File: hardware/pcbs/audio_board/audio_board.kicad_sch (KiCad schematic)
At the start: 16 parts, among them J11 Conn_01x08, J4 NC3MAH, J5 NC3MAH, J6 AudioJack3, J8 I2C

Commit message: fix libraries
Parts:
- removed U4: ~, Library:Teensy41, symbol Parts:Teensy41
- added R7, R8: 47, Resistor_SMD:R_0805_2012Metric, symbol Device:R
- added U1: ~, extra:Teensy41, symbol extra:Teensy41
- J2: renamed from J11; footprint Library:mta100_01x8_P2.54_647050-8 -> Connector_MTA-100:mta100_01x8_P2.54_647050-8
- renumbered H3 to H2, H2 to H3, J8 to J1, J4 to J3, J6 to J4, R11 to R1, R12 to R2, R13 to R3, R14 to R4, R71 to R5, R72 to R6
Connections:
- net +3V3 is gone; now on net +3.3V: J1.1 (Pin_1), J2.8 (Pin_8), R1.1, R2.1, R3.1, R4.1
- net +3.3V: now also U1.3V (3v3)
- net +5V: now also U1.5V (Vin)
- net CS_LEFT: now also U1.9
- net CS_RIGHT: now also U1.10
- net DC: now also U1.12
- net DECT_INT: now also U1.33
- net DECT_RESET: now also U1.34
- net DECT_RX: now also U1.15
- net DECT_TX: now also U1.14
- net GND: now also U1.G (GND)
- net HP_GND: now also R8.1; no longer J4.S
- net I2S1_BCLK: now also U1.21
- net I2S1_LRCLK: now also U1.20
- net I2S1_MCLK: now also U1.23
- net I2S1_RX1: now also U1.8
- net I2S1_RX2: now also U1.6
- net I2S1_TX1: now also U1.7
- net I2S1_TX2: now also U1.32
- net I2S2_BCLK: now also U1.4
- net I2S2_FS: now also U1.3
- net I2S2_RX: now also U1.5
- net I2S2_TX: now also U1.2
- net MOSI: now also U1.11
- net PHANTOM_IN1_EN: now also U1.37
- net PHANTOM_IN2_EN: now also U1.36
- net PHANTOM_IN3_EN: now also U1.35
- net RESET: now also U1.24
- net SCK: now also U1.13
- net SCL: now also U1.19
- net SCL1: now also U1.16
- net SDA: now also U1.18
- net SDA1: now also U1.17
- new net: J4.S, R7.2, R8.2
- new net DAC 2/OUTA-: R7.1
- no-connect marks 2 -> 23
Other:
- moved on the sheet: J1, J2, J3, J4, J5, R1, R2, R3, R4, R5, R6

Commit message: final touches to libraries
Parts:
- J3, J5: footprint Library:Jack_XLR_Neutrik_NC3MAH_Horizontal -> conn:Jack_XLR_Neutrik_NC3MAH_Horizontal
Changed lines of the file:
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@@
 			)
 		)
-		(property "Footprint" "Library:Jack_XLR_Neutrik_NC3MAH_Horizontal"
+		(property "Footprint" "conn:Jack_XLR_Neutrik_NC3MAH_Horizontal"
 			(at 212.09 85.09 0)
 			(effects
@@
 			)
 		)
-		(property "Footprint" "Library:Jack_XLR_Neutrik_NC3MAH_Horizontal"
+		(property "Footprint" "conn:Jack_XLR_Neutrik_NC3MAH_Horizontal"
 			(at 184.15 85.09 0)
 			(effects

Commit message: some more routing
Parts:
- added R9: 0, Resistor_SMD:R_0805_2012Metric, symbol Device:R
- R7, R8: value 47 -> 0
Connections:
- net GND: now also R9.1
- net at J4.S, R7.2, R8.2: now also R9.2
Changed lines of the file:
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@@
 	(text "OUTB- close to connector"
 		(exclude_from_sim no)
-		(at 185.166 143.51 0)
+		(at 191.77 128.27 0)
 		(effects
 			(font
@@
 	(wire
 		(pts
+			(xy 177.8 148.59) (xy 177.8 149.86)
+		)
+		(stroke
+			(width 0)
+			(type default)
+		)
+	)
+	(wire
+		(pts
 			(xy 25.4 80.01) (xy 35.56 80.01)
 		)
@@
 	(wire
 		(pts
+			(xy 177.8 138.43) (xy 177.8 140.97)
+		)
+		(stroke
+			(width 0)
+			(type default)
+		)
+	)
+	(wire
+		(pts
 			(xy 25.4 69.85) (xy 35.56 69.85)
 		)
@@
 	(symbol
 		(lib_id "power:GND")
+		(at 177.8 149.86 0)
+		(unit 1)
+		(exclude_from_sim no)
+		(in_bom yes)
+		(on_board yes)
+		(dnp no)
+		(fields_autoplaced yes)
+		(property "Reference" "#PWR013"
+			(at 177.8 156.21 0)
+			(effects
+				(font
+					(size 1.27 1.27)
+				)
+				(hide yes)
+			)
+		)
+		(property "Value" "GND"
+			(at 177.8 154.3034 0)
+			(effects
+				(font
+					(size 1.27 1.27)
+				)
+				(hide yes)
+			)
+		)
+		(property "Footprint" ""
+			(at 177.8 149.86 0)
+			(effects
+				(font
+					(size 1.27 1.27)
+				)
+				(hide yes)
+			)
+		)
+		(property "Datasheet" ""
+			(at 177.8 149.86 0)
+			(effects
+				(font
+					(size 1.27 1.27)
+				)
+				(hide yes)
+			)
+		)
+		(property "Description" ""
+			(at 177.8 149.86 0)
+			(effects
+				(font
+					(size 1.27 1.27)
+				)
+				(hide yes)
+			)
+		)
+		(pin "1"
+		)
+		(instances
+			(project "audio_board"
+				(path "/54443f96-c7c5-4432-b890-45b14a1547a1"
+					(reference "#PWR013")
+					(unit 1)
+				)
+			)
+		)
+	)
+	(symbol
+		(lib_id "power:GND")
 		(at 165.1 67.31 0)
 		(unit 1)
@@
 		(dnp no)
 		(fields_autoplaced yes)
-		(property "Reference" "#PWR016"
+		(property "Reference" "#PWR017"
 			(at 259.08 144.78 0)
 			(effects
@@
 			(project "audio_board"
 				(path "/54443f96-c7c5-4432-b890-45b14a1547a1"
-					(reference "#PWR016")
+					(reference "#PWR017")
 					(unit 1)
 				)
@@
 		(dnp no)
 		(fields_autoplaced yes)
-		(property "Reference" "#PWR017"
+		(property "Reference" "#PWR018"
 			(at 259.08 157.48 0)
 			(effects
@@
 			(project "audio_board"
 				(path "/54443f96-c7c5-4432-b890-45b14a1547a1"
-					(reference "#PWR017")
+					(reference "#PWR018")
 					(unit 1)
 				)
@@
 		(dnp no)
 		(fields_autoplaced yes)
-		(property "Reference" "#PWR015"
+		(property "Reference" "#PWR016"
 			(at 234.95 157.48 0)
 			(effects
@@
 			(project "audio_board"
 				(path "/54443f96-c7c5-4432-b890-45b14a1547a1"
-					(reference "#PWR015")
+					(reference "#PWR016")
 					(unit 1)
 				)
@@
 			)
 		)
-		(property "Value" "47"
+		(property "Value" "0"
 			(at 171.196 133.35 90)
 			(effects
@@
 		(dnp no)
 		(fields_autoplaced yes)
-		(property "Reference" "#PWR013"
+		(property "Reference" "#PWR014"
 			(at 203.2 101.6 0)
 			(effects
@@
 			(project "audio_board"
 				(path "/54443f96-c7c5-4432-b890-45b14a1547a1"
-					(reference "#PWR013")
+					(reference "#PWR014")
 					(unit 1)
 				)
@@
 		(dnp no)
 		(fields_autoplaced yes)
-		(property "Reference" "#PWR014"
+		(property "Reference" "#PWR015"
 			(at 234.95 144.78 0)
 			(effects
@@
 			(project "audio_board"
 				(path "/54443f96-c7c5-4432-b890-45b14a1547a1"
-					(reference "#PWR014")
+					(reference "#PWR015")
 					(unit 1)
 				)
@@
 	(symbol
 		(lib_id "Device:R")
+		(at 177.8 144.78 180)
+		(unit 1)
+		(exclude_from_sim no)
+		(in_bom yes)
+		(on_board yes)
+		(dnp yes)
+		(property "Reference" "R9"
+			(at 180.34 143.51 0)
+			(effects
+				(font
+					(size 1.27 1.27)
+				)
+			)
+		)
+		(property "Value" "0"
+			(at 180.34 146.05 0)
+			(effects
+				(font
+					(size 1.27 1.27)
+				)
+			)
+		)
+		(property "Footprint" "Resistor_SMD:R_0805_2012Metric"
+			(at 179.578 144.78 90)
+			(effects
+				(font
+					(size 1.27 1.27)
+				)
+				(hide yes)
+			)
+		)
+		(property "Datasheet" "~"
+			(at 177.8 144.78 0)
+			(effects
+				(font
+					(size 1.27 1.27)
+				)
+				(hide yes)
+			)
+		)
+		(property "Description" "Resistor"
+			(at 177.8 144.78 0)
+			(effects
+				(font
+					(size 1.27 1.27)
+				)
+				(hide yes)
+			)
+		)
+		(property "LCSC" "C23182"
+			(at 177.8 144.78 0)
+			(effects
+				(font
+					(size 1.27 1.27)
+				)
+				(hide yes)
+			)
+		)
+		(property "MPN" "560112116054"
+			(at 177.8 144.78 0)
+			(effects
+				(font
+					(size 1.27 1.27)
+				)
+				(hide yes)
+			)
+		)
+		(property "Part" "R 47Ω 125mW 1% 0603"
+			(at 177.8 144.78 0)
+			(effects
+				(font
+					(size 1.27 1.27)
+				)
+				(hide yes)
+			)
+		)
+		(property "Shop" "https://store.comet.bg/Catalogue/Product/4392/"
+			(at 177.8 144.78 0)
+			(effects
+				(font
+					(size 1.27 1.27)
+				)
+				(hide yes)
+			)
+		)
+		(pin "1"
+		)
+		(pin "2"
+		)
+		(instances
+			(project "audio_board"
+				(path "/54443f96-c7c5-4432-b890-45b14a1547a1"
+					(reference "R9")
+					(unit 1)
+				)
+			)
+		)
+	)
+	(symbol
+		(lib_id "Device:R")
 		(at 171.45 138.43 90)
 		(unit 1)
@@
 			)
 		)
-		(property "Value" "47"
+		(property "Value" "0"
 			(at 171.196 138.43 90)
 			(effects

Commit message: route some more
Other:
- sheet PC Mono input ports: added OUT+, OUT-; removed OUTPUT
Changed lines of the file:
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@@
 	(wire
 		(pts
+			(xy 165.1 63.5) (xy 187.96 63.5)
+		)
+		(stroke
+			(width 0)
+			(type default)
+		)
+	)
+	(wire
+		(pts
 			(xy 44.45 22.86) (xy 44.45 24.13)
 		)
@@
 	(wire
 		(pts
-			(xy 165.1 46.99) (xy 165.1 67.31)
+			(xy 165.1 46.99) (xy 165.1 63.5)
 		)
 		(stroke
@@
 		(dnp no)
 		(fields_autoplaced yes)
-		(property "Reference" "#PWR013"
+		(property "Reference" "#PWR012"
 			(at 177.8 156.21 0)
 			(effects
@@
 			(project "audio_board"
 				(path "/54443f96-c7c5-4432-b890-45b14a1547a1"
-					(reference "#PWR013")
-					(unit 1)
-				)
-			)
-		)
-	)
-	(symbol
-		(lib_id "power:GND")
-		(at 165.1 67.31 0)
-		(unit 1)
-		(exclude_from_sim no)
-		(in_bom yes)
-		(on_board yes)
-		(dnp no)
-		(fields_autoplaced yes)
-		(property "Reference" "#PWR011"
-			(at 165.1 73.66 0)
-			(effects
-				(font
-					(size 1.27 1.27)
-				)
-				(hide yes)
-			)
-		)
-		(property "Value" "GND"
-			(at 165.1 72.39 0)
-			(effects
-				(font
-					(size 1.27 1.27)
-				)
-				(hide yes)
-			)
-		)
-		(property "Footprint" ""
-			(at 165.1 67.31 0)
-			(effects
-				(font
-					(size 1.27 1.27)
-				)
-				(hide yes)
-			)
-		)
-		(property "Datasheet" ""
-			(at 165.1 67.31 0)
-			(effects
-				(font
-					(size 1.27 1.27)
-				)
-				(hide yes)
-			)
-		)
-		(property "Description" "Power symbol creates a global label with name \"GND\" , ground"
-			(at 165.1 67.31 0)
-			(effects
-				(font
-					(size 1.27 1.27)
-				)
-				(hide yes)
-			)
-		)
-		(pin "1"
-		)
-		(instances
-			(project ""
-				(path "/54443f96-c7c5-4432-b890-45b14a1547a1"
-					(reference "#PWR011")
+					(reference "#PWR012")
 					(unit 1)
 				)
@@
 		(dnp no)
 		(fields_autoplaced yes)
-		(property "Reference" "#PWR017"
+		(property "Reference" "#PWR016"
 			(at 259.08 144.78 0)
 			(effects
@@
 			(project "audio_board"
 				(path "/54443f96-c7c5-4432-b890-45b14a1547a1"
-					(reference "#PWR017")
+					(reference "#PWR016")
 					(unit 1)
 				)
@@
 		(dnp no)
 		(fields_autoplaced yes)
-		(property "Reference" "#PWR018"
+		(property "Reference" "#PWR017"
 			(at 259.08 157.48 0)
 			(effects
@@
 			(project "audio_board"
 				(path "/54443f96-c7c5-4432-b890-45b14a1547a1"
-					(reference "#PWR018")
+					(reference "#PWR017")
 					(unit 1)
 				)
@@
 		(dnp no)
 		(fields_autoplaced yes)
-		(property "Reference" "#PWR012"
+		(property "Reference" "#PWR011"
 			(at 175.26 101.6 0)
 			(effects
@@
 			(project "audio_board"
 				(path "/54443f96-c7c5-4432-b890-45b14a1547a1"
-					(reference "#PWR012")
+					(reference "#PWR011")
 					(unit 1)
 				)
@@
 		(dnp no)
 		(fields_autoplaced yes)
-		(property "Reference" "#PWR016"
+		(property "Reference" "#PWR015"
 			(at 234.95 157.48 0)
 			(effects
@@
 			(project "audio_board"
 				(path "/54443f96-c7c5-4432-b890-45b14a1547a1"
-					(reference "#PWR016")
+					(reference "#PWR015")
 					(unit 1)
 				)
@@
 		(dnp no)
 		(fields_autoplaced yes)
-		(property "Reference" "#PWR014"
+		(property "Reference" "#PWR013"
 			(at 203.2 101.6 0)
 			(effects
@@
 			(project "audio_board"
 				(path "/54443f96-c7c5-4432-b890-45b14a1547a1"
-					(reference "#PWR014")
+					(reference "#PWR013")
 					(unit 1)
 				)
@@
 		(dnp no)
 		(fields_autoplaced yes)
-		(property "Reference" "#PWR015"
+		(property "Reference" "#PWR014"
 			(at 234.95 144.78 0)
 			(effects
@@
 			(project "audio_board"
 				(path "/54443f96-c7c5-4432-b890-45b14a1547a1"
-					(reference "#PWR015")
+					(reference "#PWR014")
 					(unit 1)
 				)
@@
 	)
 	(sheet
-		(at 187.96 34.925)
+		(at 187.96 23.495)
 		(size 31.75 6.35)
 		(exclude_from_sim no)
@@
 		)
 		(property "Sheetname" "XLR input 2"
-			(at 187.96 34.2134 0)
+			(at 187.96 22.7834 0)
 			(effects
 				(font
@@
 		)
 		(property "Sheetfile" "xlr_input.kicad_sch"
-			(at 187.96 41.8596 0)
+			(at 187.96 30.4296 0)
 			(effects
 				(font
@@
 		)
 		(pin "COLD" output
-			(at 187.96 39.37 180)
+			(at 187.96 27.94 180)
 			(effects
 				(font
@@
 		)
 		(pin "HOT" output
-			(at 187.96 36.83 180)
+			(at 187.96 25.4 180)
 			(effects
 				(font
@@
 		)
 		(pin "PHANTOM_PULLDOWN" input
-			(at 219.71 36.83 0)
+			(at 219.71 25.4 0)
 			(effects
 				(font
@@
 	)
 	(sheet
-		(at 187.96 23.495)
+		(at 187.96 34.925)
 		(size 31.75 6.35)
 		(exclude_from_sim no)
@@
 		)
 		(property "Sheetname" "XLR input 1"
-			(at 187.96 22.7834 0)
+			(at 187.96 34.2134 0)
 			(effects
 				(font
@@
 		)
 		(property "Sheetfile" "xlr_input.kicad_sch"
-			(at 187.96 30.4296 0)
+			(at 187.96 41.8596 0)
 			(effects
 				(font
@@
 		)
 		(pin "COLD" output
-			(at 187.96 27.94 180)
+			(at 187.96 39.37 180)
 			(effects
 				(font
@@
 		)
 		(pin "HOT" output
-			(at 187.96 25.4 180)
+			(at 187.96 36.83 180)
 			(effects
 				(font
@@
 		)
 		(pin "PHANTOM_PULLDOWN" input
-			(at 219.71 25.4 0)
+			(at 219.71 36.83 0)
 			(effects
 				(font
@@
 	(sheet
 		(at 187.96 58.42)
-		(size 24.13 5.08)
+		(size 24.13 7.62)
 		(exclude_from_sim no)
 		(in_bom yes)
@@
 		)
 		(property "Sheetfile" "input_mono.kicad_sch"
-			(at 187.96 64.0846 0)
+			(at 187.96 66.6246 0)
 			(effects
 				(font
@@
 			)
 		)
-		(pin "OUTPUT" output
+		(pin "OUT+" output
 			(at 187.96 60.96 180)
 			(effects
 				(font
+					(size 1.27 1.27)
+				)
+				(justify left)
+			)
+		)
+		(pin "OUT-" output
+			(at 187.96 63.5 180)
+			(effects
+				(font

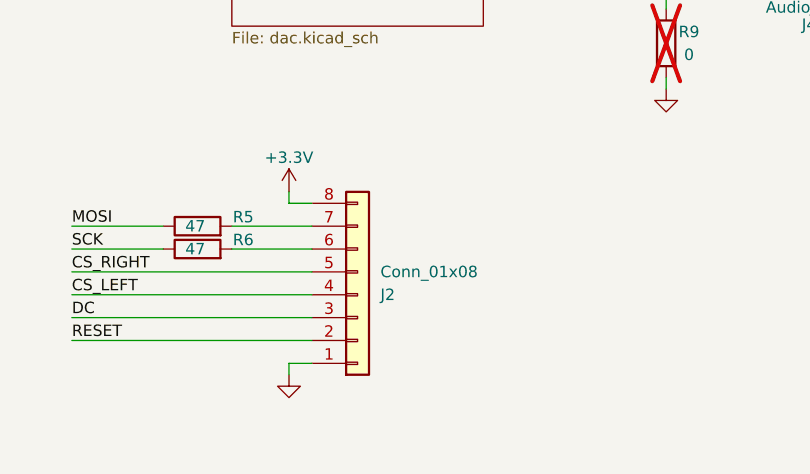
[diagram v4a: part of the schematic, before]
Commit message: fix XLR courtyard
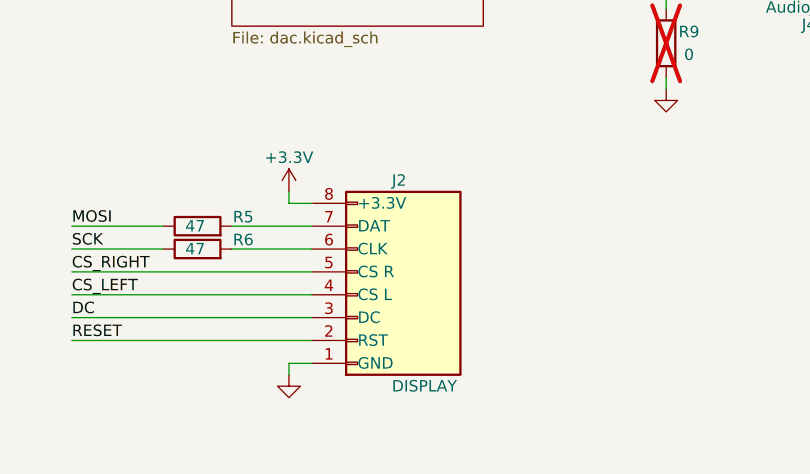
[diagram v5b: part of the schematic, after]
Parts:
- removed J2: Conn_01x08, Connector_MTA-100:mta100_01x8_P2.54_647050-8, symbol Connector_Generic:Conn_01x08
- added J2: MTA100_08, Connector_MTA-100:mta100_01x8_P2.54_647050-8, symbol conn:Conn_01x08
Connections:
- net +3.3V: now also J2.8 (Pin_8)
- net CS_LEFT: now also J2.4 (Pin_4)
- net CS_RIGHT: now also J2.5 (Pin_5)
- net DC: now also J2.3 (Pin_3)
- net GND: now also J2.1 (Pin_1)
- net RESET: now also J2.2 (Pin_2)
- net at R6.2: now also J2.6 (Pin_6)
- net at R5.2: now also J2.7 (Pin_7)
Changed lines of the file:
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@@
+	)
+	(symbol
+		(lib_id "conn:Conn_01x08")
+		(at 143.51 177.8 0)
+		(mirror x)
+		(unit 1)
+		(exclude_from_sim no)
+		(in_bom yes)
+		(on_board yes)
+		(dnp no)
+		(property "Reference" "J2"
+			(at 147.32 160.02 0)
+			(effects
+				(font
+					(size 1.27 1.27)
+				)
+				(justify left)
+			)
+		)
+		(property "Value" "MTA100_08"
+			(at 148.336 160.02 0)
+			(effects
+				(font
+					(size 1.27 1.27)
+				)
+				(hide yes)
+			)
+		)
+		(property "Footprint" "Connector_MTA-100:mta100_01x8_P2.54_647050-8"
+			(at 143.51 182.118 0)
+			(effects
+				(font
+					(size 1.27 1.27)
+				)
+				(hide yes)
+			)
+		)
+		(property "Datasheet" "~"
+			(at 143.51 177.8 0)
+			(effects
+				(font
+					(size 1.27 1.27)
+				)
+				(hide yes)
+			)
+		)
+		(property "Description" "Generic connector, single row, 01x06, script generated (kicad-library-utils/schlib/autogen/connector/)"
+			(at 143.764 182.118 0)
+			(effects
+				(font
+					(size 1.27 1.27)
+				)
+				(hide yes)
+			)
+		)
+		(property "Purpose Pin1" "GND"
+			(at 143.51 180.34 0)
+			(do_not_autoplace yes)
+			(effects
+				(font
+					(size 1.27 1.27)
+				)
+				(justify left)
+			)
+		)
+		(property "Purpose Pin2" "RST"
+			(at 143.51 177.8 0)
+			(do_not_autoplace yes)
+			(effects
+				(font
+					(size 1.27 1.27)
+				)
+				(justify left)
+			)
+		)
+		(property "Purpose Pin3" "DC"
+			(at 143.51 175.26 0)
+			(do_not_autoplace yes)
+			(effects
+				(font
+					(size 1.27 1.27)
+				)
+				(justify left)
+			)
+		)
+		(property "Purpose Pin4" "CS L"
+			(at 143.51 172.72 0)
+			(do_not_autoplace yes)
+			(effects
+				(font
+					(size 1.27 1.27)
+				)
+				(justify left)
+			)
+		)
+		(property "Purpose Pin5" "CS R"
+			(at 143.51 170.18 0)
+			(do_not_autoplace yes)
+			(effects
+				(font
+					(size 1.27 1.27)
+				)
+				(justify left)
+			)
+		)
+		(property "Purpose Pin6" "CLK"
+			(at 143.51 167.64 0)
+			(do_not_autoplace yes)
+			(effects
+				(font
+					(size 1.27 1.27)
+				)
+				(justify left)
+			)
+		)
+		(property "Purpose Pin7" "DAT"
+			(at 143.51 165.1 0)
+			(do_not_autoplace yes)
+			(effects
+				(font
+					(size 1.27 1.27)
+				)
+				(justify left)
+			)
+		)
+		(property "Purpose Pin8" "+3.3V"
+			(at 143.51 162.56 0)
+			(do_not_autoplace yes)
+			(effects
+				(font
+					(size 1.27 1.27)
+				)
+				(justify left)
+			)
+		)
+		(property "Purpose" "DISPLAY"
+			(at 147.32 182.88 0)
+			(effects
+				(font
+					(size 1.27 1.27)
+				)
+				(justify left)
+			)
+		)
+		(property "Part" "640457-8"
+			(at 143.51 177.8 0)
+			(effects
+				(font
+					(size 1.27 1.27)
+				)
+				(hide yes)
+			)
+		)
+		(property "Shop" "https://eu.mouser.com/ProductDetail/TE-Connectivity/640457-8?qs=%2F35zJ5USjokX8LSglMnOhw%3D%3D"
+			(at 143.51 177.8 0)
+			(effects
+				(font
+					(size 1.27 1.27)
+				)
+				(hide yes)
+			)
+		)
+		(pin "6"
+		)
+		(pin "7"
+		)
+		(pin "1"
+		)
+		(pin "4"
+		)
+		(pin "3"
+		)
+		(pin "8"
+		)
+		(pin "2"
+		)
+		(pin "5"
+		)
+		(instances
+			(project "audio_board"
+				(path "/54443f96-c7c5-4432-b890-45b14a1547a1"
+					(reference "J2")
+					(unit 1)
+				)
+			)
+		)
 	)
 	(symbol
@@
 					(unit 1)
 				)
-			)
-		)
-	)
-	(symbol
-		(lib_id "Connector_Generic:Conn_01x08")
-		(at 143.51 172.72 0)
-		(mirror x)
-		(unit 1)
-		(exclude_from_sim no)
-		(in_bom yes)
-		(on_board yes)
-		(dnp no)
-		(property "Reference" "J2"
-			(at 146.05 172.7201 0)
-			(effects
-				(font
-					(size 1.27 1.27)
-				)
-				(justify left)
-			)
-		)
-		(property "Value" "Conn_01x08"
-			(at 146.05 170.1801 0)
-			(effects
-				(font
-					(size 1.27 1.27)
-				)
-				(justify left)
-			)
-		)
-		(property "Footprint" "Connector_MTA-100:mta100_01x8_P2.54_647050-8"
-			(at 143.51 172.72 0)
-			(effects
-				(font
-					(size 1.27 1.27)
-				)
-				(hide yes)
-			)
-		)
-		(property "Datasheet" "~"
-			(at 143.51 172.72 0)
-			(effects
-				(font
-					(size 1.27 1.27)
-				)
-				(hide yes)
-			)
-		)
-		(property "Description" "Generic connector, single row, 01x08, script generated (kicad-library-utils/schlib/autogen/connector/)"
-			(at 143.51 172.72 0)
-			(effects
-				(font
-					(size 1.27 1.27)
-				)
-				(hide yes)
-			)
-		)
-		(property "MPN" "640456-8"
-			(at 143.51 172.72 0)
-			(effects
-				(font
-					(size 1.27 1.27)
-				)
-				(hide yes)
-			)
-		)
-		(property "Shop" "https://eu.mouser.com/ProductDetail/TE-Connectivity-AMP/640456-8?qs=%2F35zJ5USjomho1287DA4QA%3D%3D"
-			(at 143.51 172.72 0)
-			(effects
-				(font
-					(size 1.27 1.27)
-				)
-				(hide yes)
-			)
-		)
-		(property "Part" "640456-8"
-			(at 143.51 172.72 0)
-			(effects
-				(font
-					(size 1.27 1.27)
-				)
-				(hide yes)
-			)
-		)
-		(property "LCSC" "C93636"
-			(at 143.51 172.72 0)
-			(effects
-				(font
-					(size 1.27 1.27)
-				)
-				(hide yes)
-			)
-		)
-		(pin "4"
-		)
-		(pin "2"
-		)
-		(pin "6"
-		)
-		(pin "1"
-		)
-		(pin "7"
-		)
-		(pin "5"
-		)
-		(pin "8"
-		)
-		(pin "3"
-		)
-		(instances
-			(project "audio_board"
-				(path "/54443f96-c7c5-4432-b890-45b14a1547a1"
-					(reference "J2")
-					(unit 1)
-				)

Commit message: finish routing
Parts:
- removed R8: 0, Resistor_SMD:R_0805_2012Metric, symbol Device:R
- renumbered R9 to R8
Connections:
- net HP_GND: now also J4.S, R7.2, R8.2
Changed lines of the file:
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@@
 	(wire
 		(pts
-			(xy 157.48 138.43) (xy 167.64 138.43)
+			(xy 157.48 138.43) (xy 177.8 138.43)
 		)
 		(stroke
@@
 	(wire
 		(pts
-			(xy 175.26 138.43) (xy 177.8 138.43)
-		)
-		(stroke
-			(width 0)
-			(type default)
-		)
-	)
-	(wire
-		(pts
 			(xy 203.2 85.09) (xy 204.47 85.09)
 		)
@@
 		(on_board yes)
 		(dnp yes)
-		(property "Reference" "R9"
+		(property "Reference" "R8"
 			(at 180.34 143.51 0)
 			(effects
@@
 			(effects
 				(font
-					(size 1.27 1.27)
-				)
-				(hide yes)
-			)
-		)
-		(pin "1"
-		)
-		(pin "2"
-		)
-		(instances
-			(project "audio_board"
-				(path "/54443f96-c7c5-4432-b890-45b14a1547a1"
-					(reference "R9")
-					(unit 1)
-				)
-			)
-		)
-	)
-	(symbol
-		(lib_id "Device:R")
-		(at 171.45 138.43 90)
-		(unit 1)
-		(exclude_from_sim no)
-		(in_bom yes)
-		(on_board yes)
-		(dnp no)
-		(property "Reference" "R8"
-			(at 175.26 137.16 90)
-			(effects
-				(font
-					(size 1.27 1.27)
-				)
-			)
-		)
-		(property "Value" "0"
-			(at 171.196 138.43 90)
-			(effects
-				(font
-					(size 1.27 1.27)
-				)
-			)
-		)
-		(property "Footprint" "Resistor_SMD:R_0805_2012Metric"
-			(at 171.45 140.208 90)
-			(effects
-				(font
-					(size 1.27 1.27)
-				)
-				(hide yes)
-			)
-		)
-		(property "Datasheet" "~"
-			(at 171.45 138.43 0)
-			(effects
-				(font
-					(size 1.27 1.27)
-				)
-				(hide yes)
-			)
-		)
-		(property "Description" "Resistor"
-			(at 171.45 138.43 0)
-			(effects
-				(font
-					(size 1.27 1.27)
-				)
-				(hide yes)
-			)
-		)
-		(property "LCSC" "C23182"
-			(at 171.45 138.43 0)
-			(effects
-				(font
-					(size 1.27 1.27)
-				)
-				(hide yes)
-			)
-		)
-		(property "MPN" "560112116054"
-			(at 171.45 138.43 0)
-			(effects
-				(font
-					(size 1.27 1.27)
-				)
-				(hide yes)
-			)
-		)
-		(property "Part" "R 47Ω 125mW 1% 0603"
-			(at 171.45 138.43 0)
-			(effects
-				(font
-					(size 1.27 1.27)
-				)
-				(hide yes)
-			)
-		)
-		(property "Shop" "https://store.comet.bg/Catalogue/Product/4392/"
-			(at 171.45 138.43 0)
-			(effects
-				(font
